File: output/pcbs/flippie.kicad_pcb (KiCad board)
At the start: 2 copper layers, 149.6 x 110.4 mm, 59 parts

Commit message: rename to flippie
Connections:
- ? pad 1: GND -> _1_1
- ? pad 2: P2 -> _1_1
- ? pad 3: P3 -> _1_2
- ? pad 4: INT -> _1_2
- ? pad 5: GND -> _1_3

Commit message: move mcu
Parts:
- moved MCU1 1.15 mm to (206.5, 42.8)

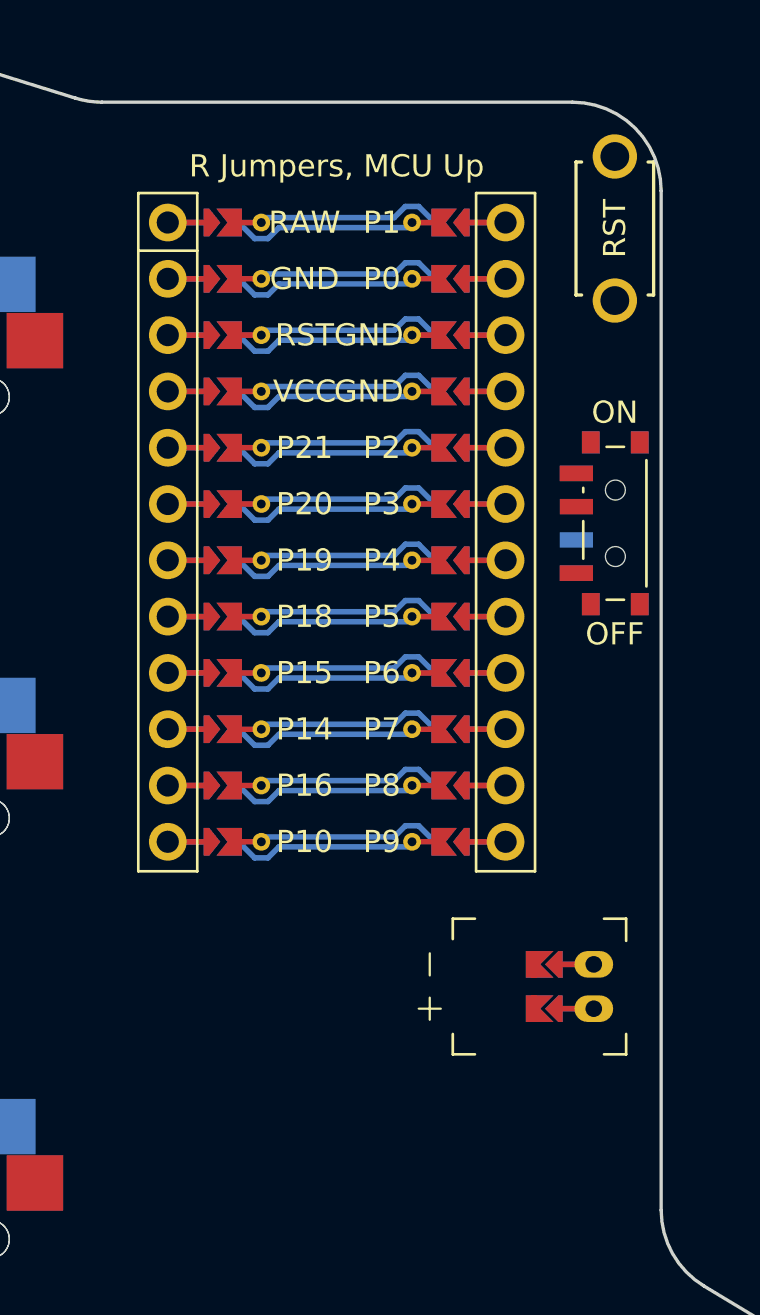
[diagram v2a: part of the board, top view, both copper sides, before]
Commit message: adding oled
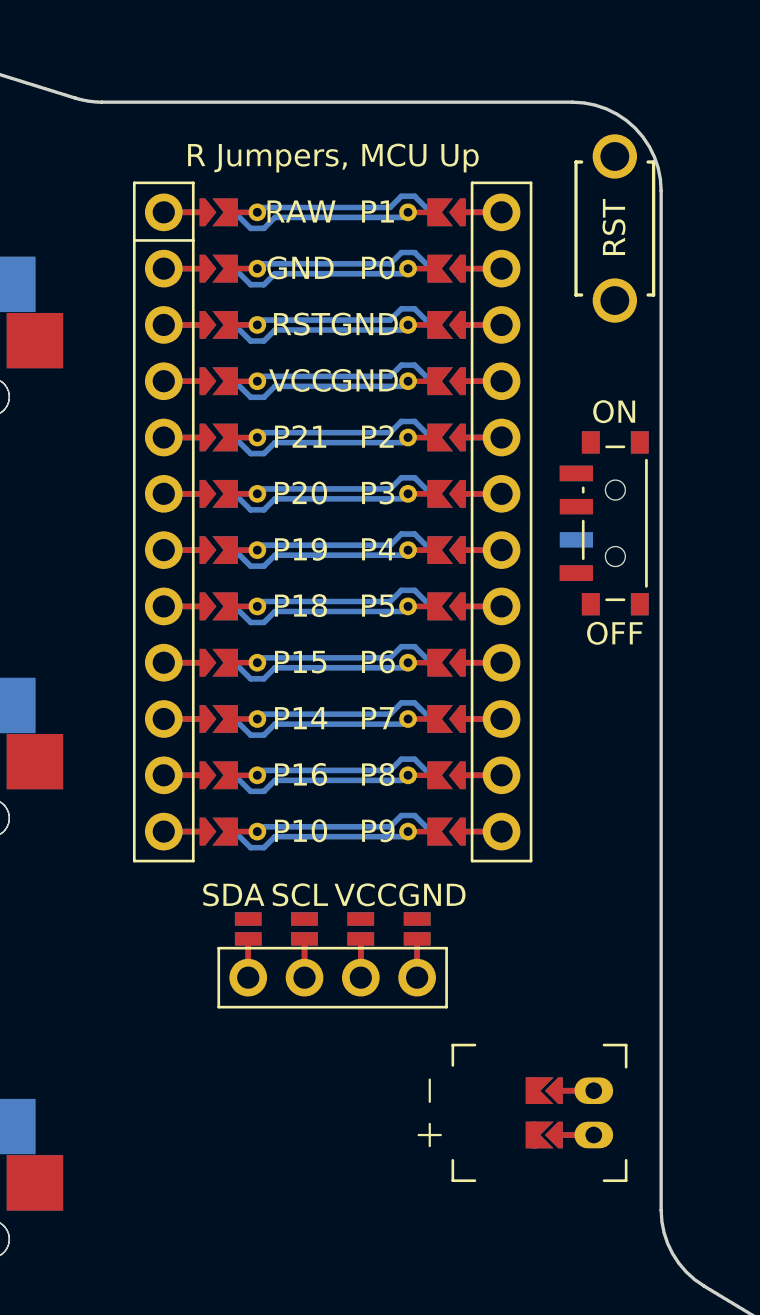
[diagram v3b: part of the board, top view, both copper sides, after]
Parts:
- added DISP1: , ceoloide:display_ssd1306, F.Cu at (206.4, 47.5)
- moved JST1 5.70 mm to (218.1, 70.3)
- moved MCU1 0.49 mm to (206.4, 42.4)
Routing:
- net VCC: track 0.00 -> 3.50 mm
- net SDA: track 0.00 -> 3.50 mm
- net SCL: track 0.00 -> 3.50 mm
- net GND: track 0.00 -> 3.50 mm

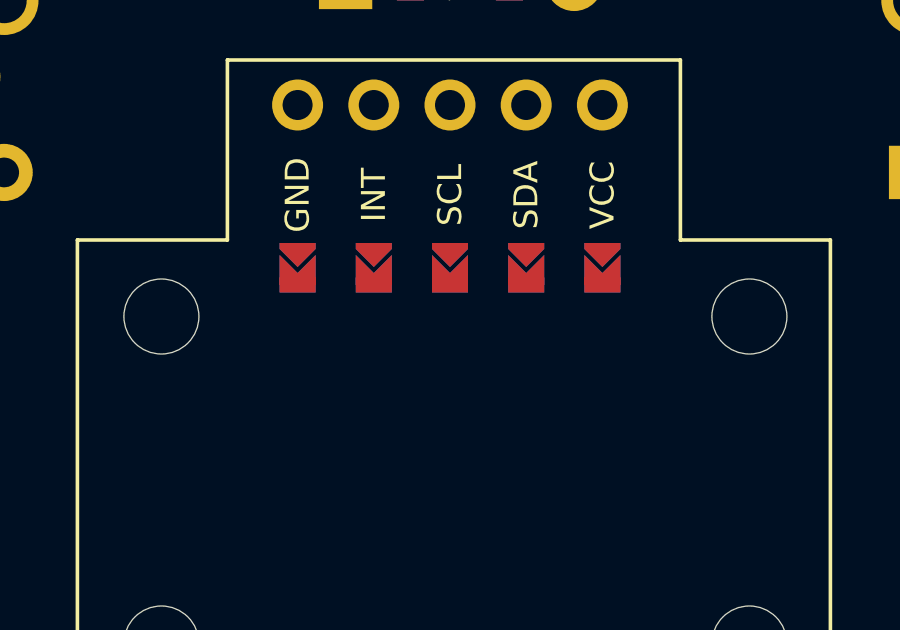
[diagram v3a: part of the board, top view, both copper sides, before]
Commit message: creating through holes for pimonori for easier routing
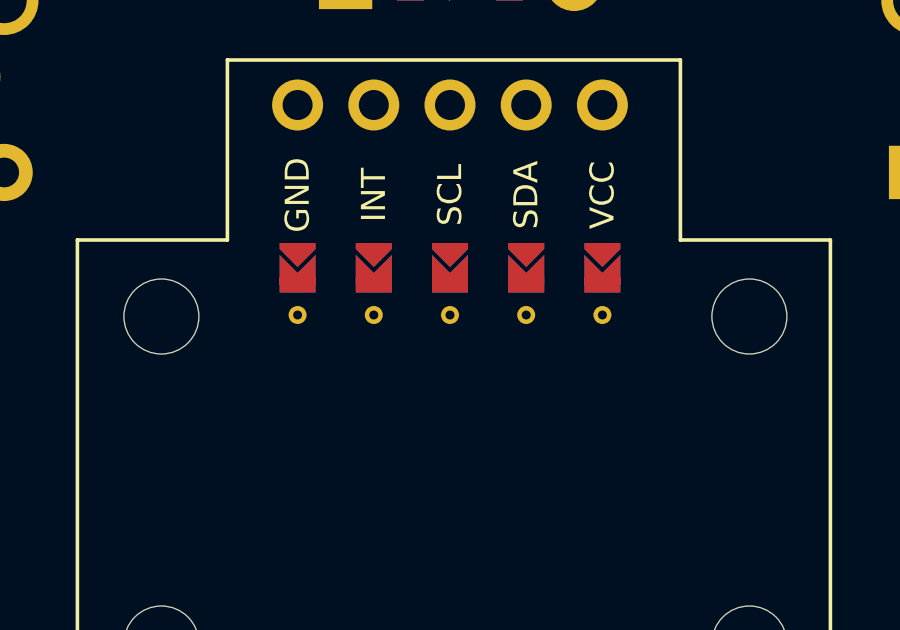
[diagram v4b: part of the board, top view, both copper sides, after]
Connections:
- ? pad 1: _1_1 -> VCC
- ? pad 2: _1_1 -> P2
- ? pad 3: _1_2 -> P3
- ? pad 4: _1_2 -> INT
- ? pad 5: _1_3 -> GND
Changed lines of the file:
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@@
             )
         )
-      )
+        (pad 1 thru_hole oval (at 7 0 0) (size 0.6 0.6) (drill 0.3) (layers *.Cu *.Mask) (net 31 "VCC"))
+        (pad 2 thru_hole oval (at 7 2.54 0) (size 0.6 0.6) (drill 0.3) (layers *.Cu *.Mask) (net 34 "P2"))
+        (pad 3 thru_hole oval (at 7 5.08 0) (size 0.6 0.6) (drill 0.3) (layers *.Cu *.Mask) (net 35 "P3"))
+        (pad 4 thru_hole oval (at 7 7.62 0) (size 0.6 0.6) (drill 0.3) (layers *.Cu *.Mask) (net 77 "INT"))
+        (pad 5 thru_hole oval (at 7 10.16 0) (size 0.6 0.6) (drill 0.3) (layers *.Cu *.Mask) (net 29 "GND"))
+    )
   (gr_line (start 101.4026967 97.6197628) (end 119.7648005 95.36518) (angle 90) (layer Eco1.User) (width 0.15))
 (gr_line (start 119.7648005 95.36518) (end 117.5102177 77.0030762) (angle 90) (layer Eco1.User) (width 0.15))

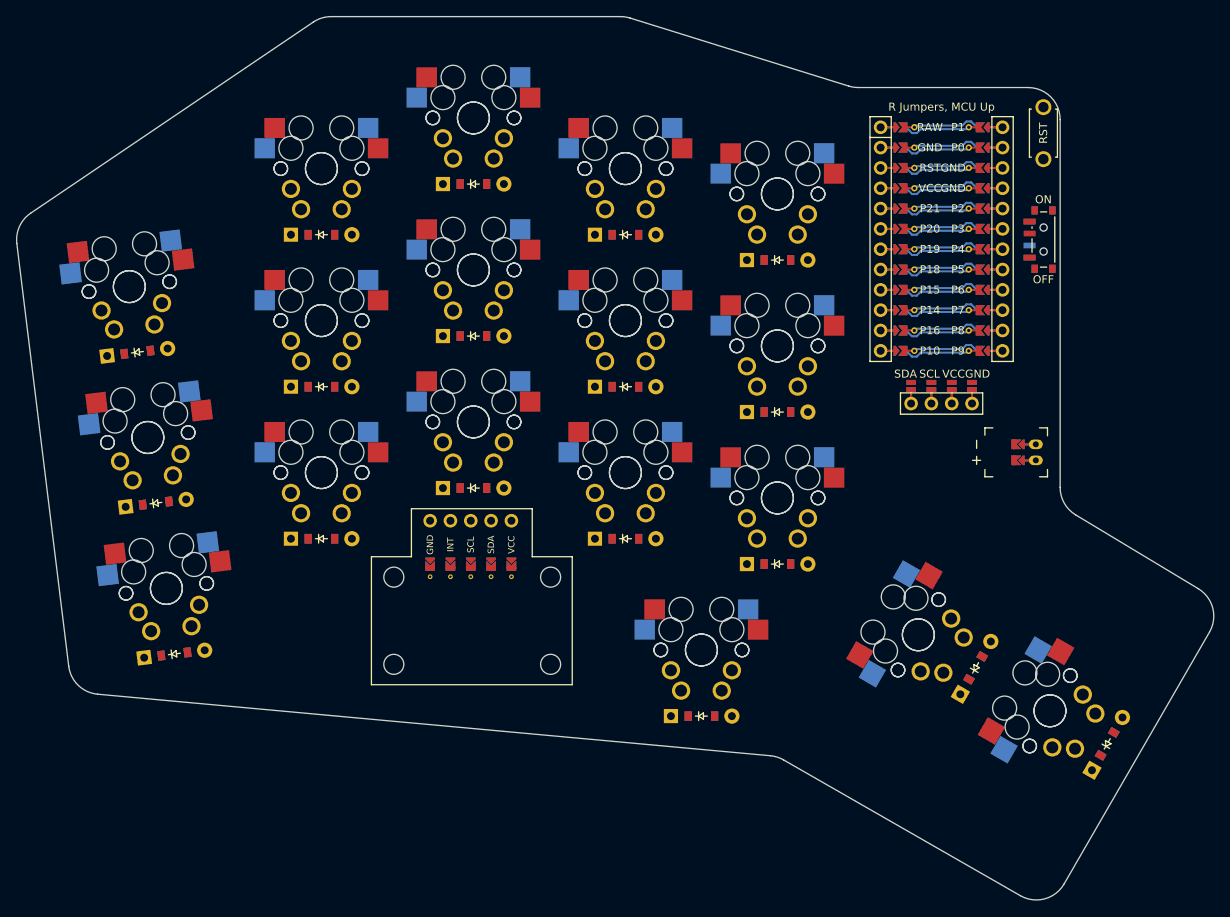
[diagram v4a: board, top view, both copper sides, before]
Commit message: adding missing traces and mounting holes
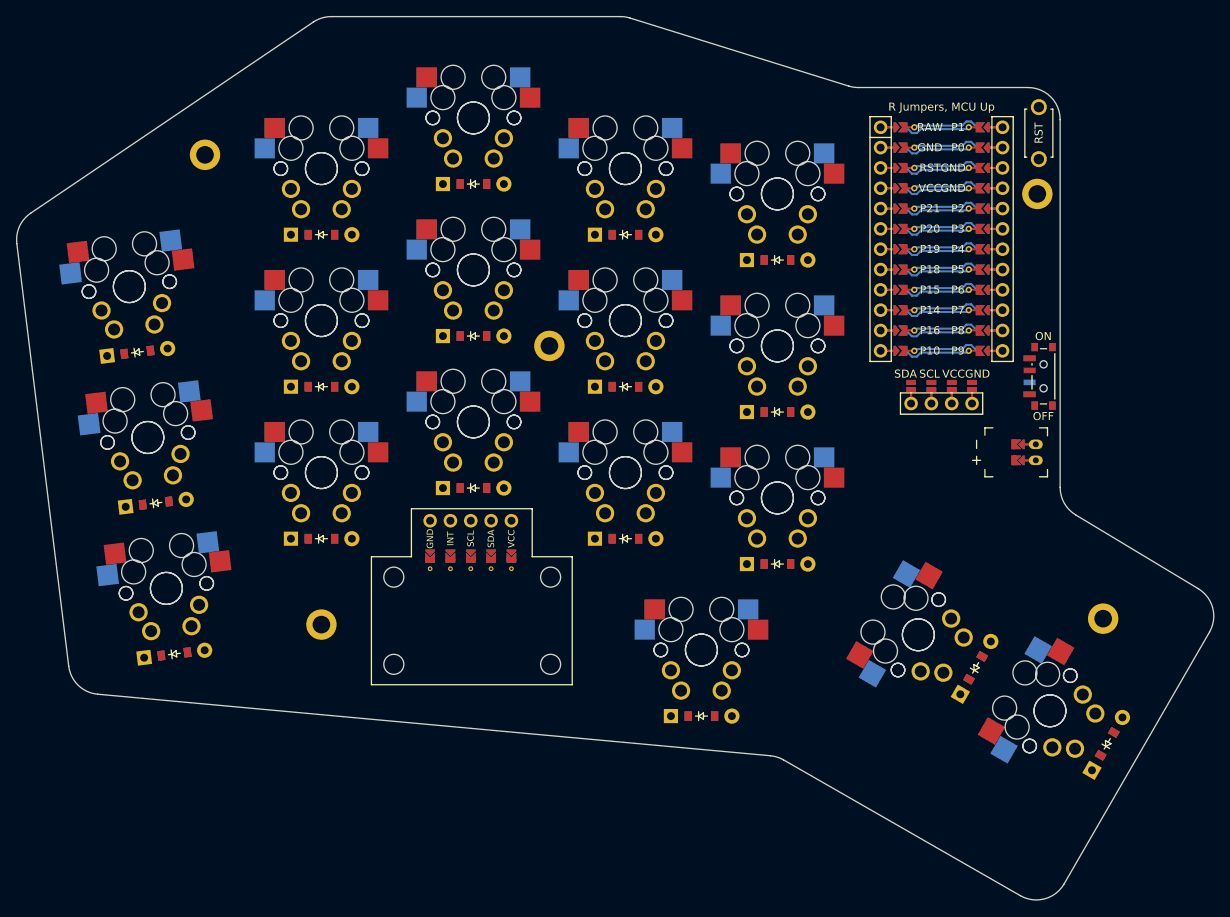
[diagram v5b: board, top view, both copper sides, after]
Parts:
- added H1: , ceoloide:mounting_hole_plated, F.Cu at (114.3, 33.1)
- added H2: , ceoloide:mounting_hole_plated, F.Cu at (218.3, 38.0)
- added H3: , ceoloide:mounting_hole_plated, F.Cu at (226.6, 91.1)
- added H4: , ceoloide:mounting_hole_plated, F.Cu at (128.8, 91.8)
- added H5: , ceoloide:mounting_hole_plated, F.Cu at (157.3, 57.0)
- moved PWR1 17.1 mm to (219.1, 60.8)
- moved RST1 0.57 mm to (218.5, 30.4)
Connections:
- DISP1 pad 16: SCL -> P3
- DISP1 pad 17: SDA -> P2
- DISP1 pad 26: SCL -> P3
- DISP1 pad 27: SDA -> P2
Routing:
- net SDA: track 3.50 -> 0.00 mm
- net SCL: track 3.50 -> 0.00 mm
- net P3: track 0.00 -> 3.50 mm
- net P2: track 0.00 -> 3.50 mm
